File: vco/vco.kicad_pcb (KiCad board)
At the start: 2 copper layers, 59 parts, among them J1 Filtered Power, J13 Octave, J2 SQUARE OUT, J3 TRIANGLE OUT, J4 RAMP OUT, J5 1V/OCT, J6 CV, J7 SYNC, J8 PWM, J9 FM, U1 TL074, U2 TL072, U3 AS3340, U4 LM4040

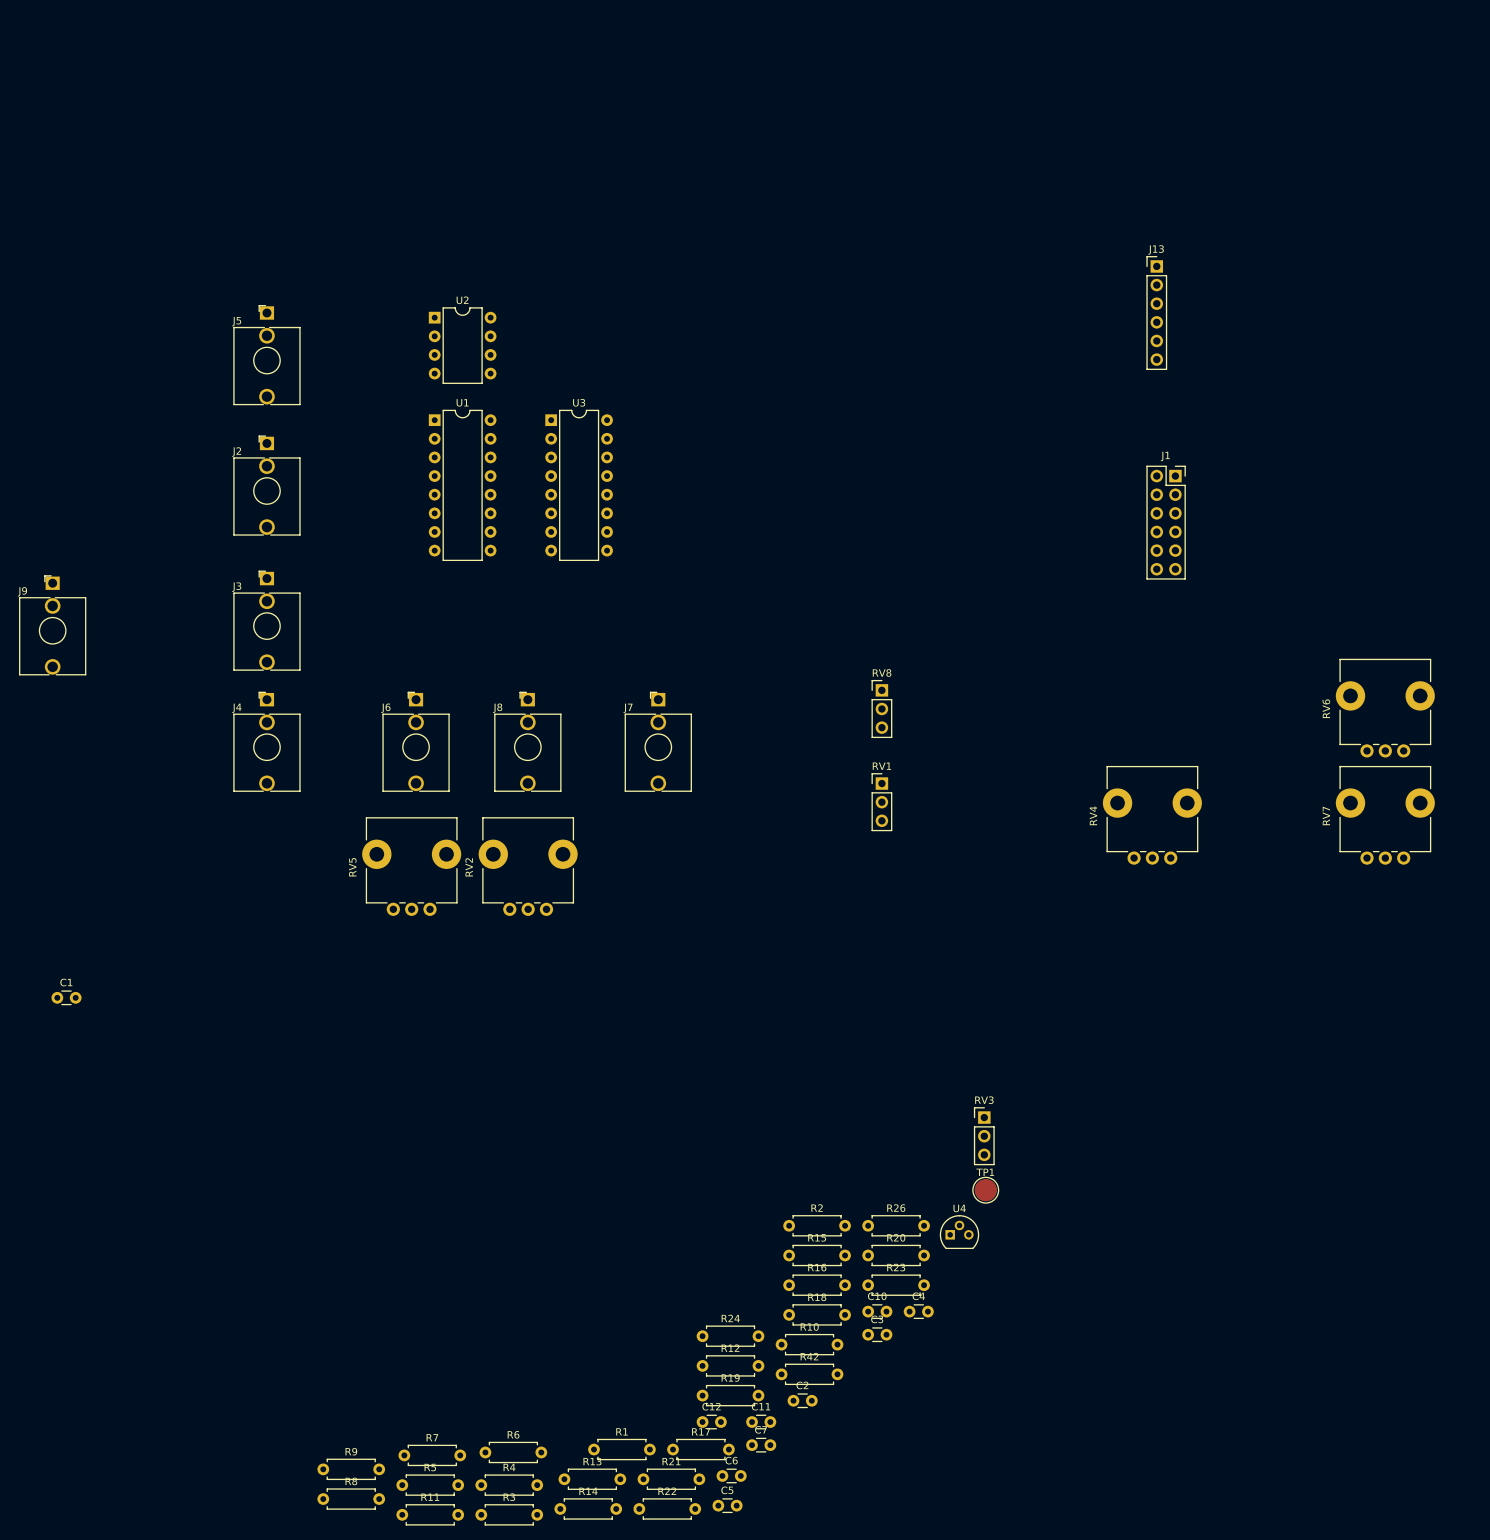
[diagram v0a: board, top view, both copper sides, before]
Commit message: Extra 7805 footprint, new standard, and some order to the VCO chaos
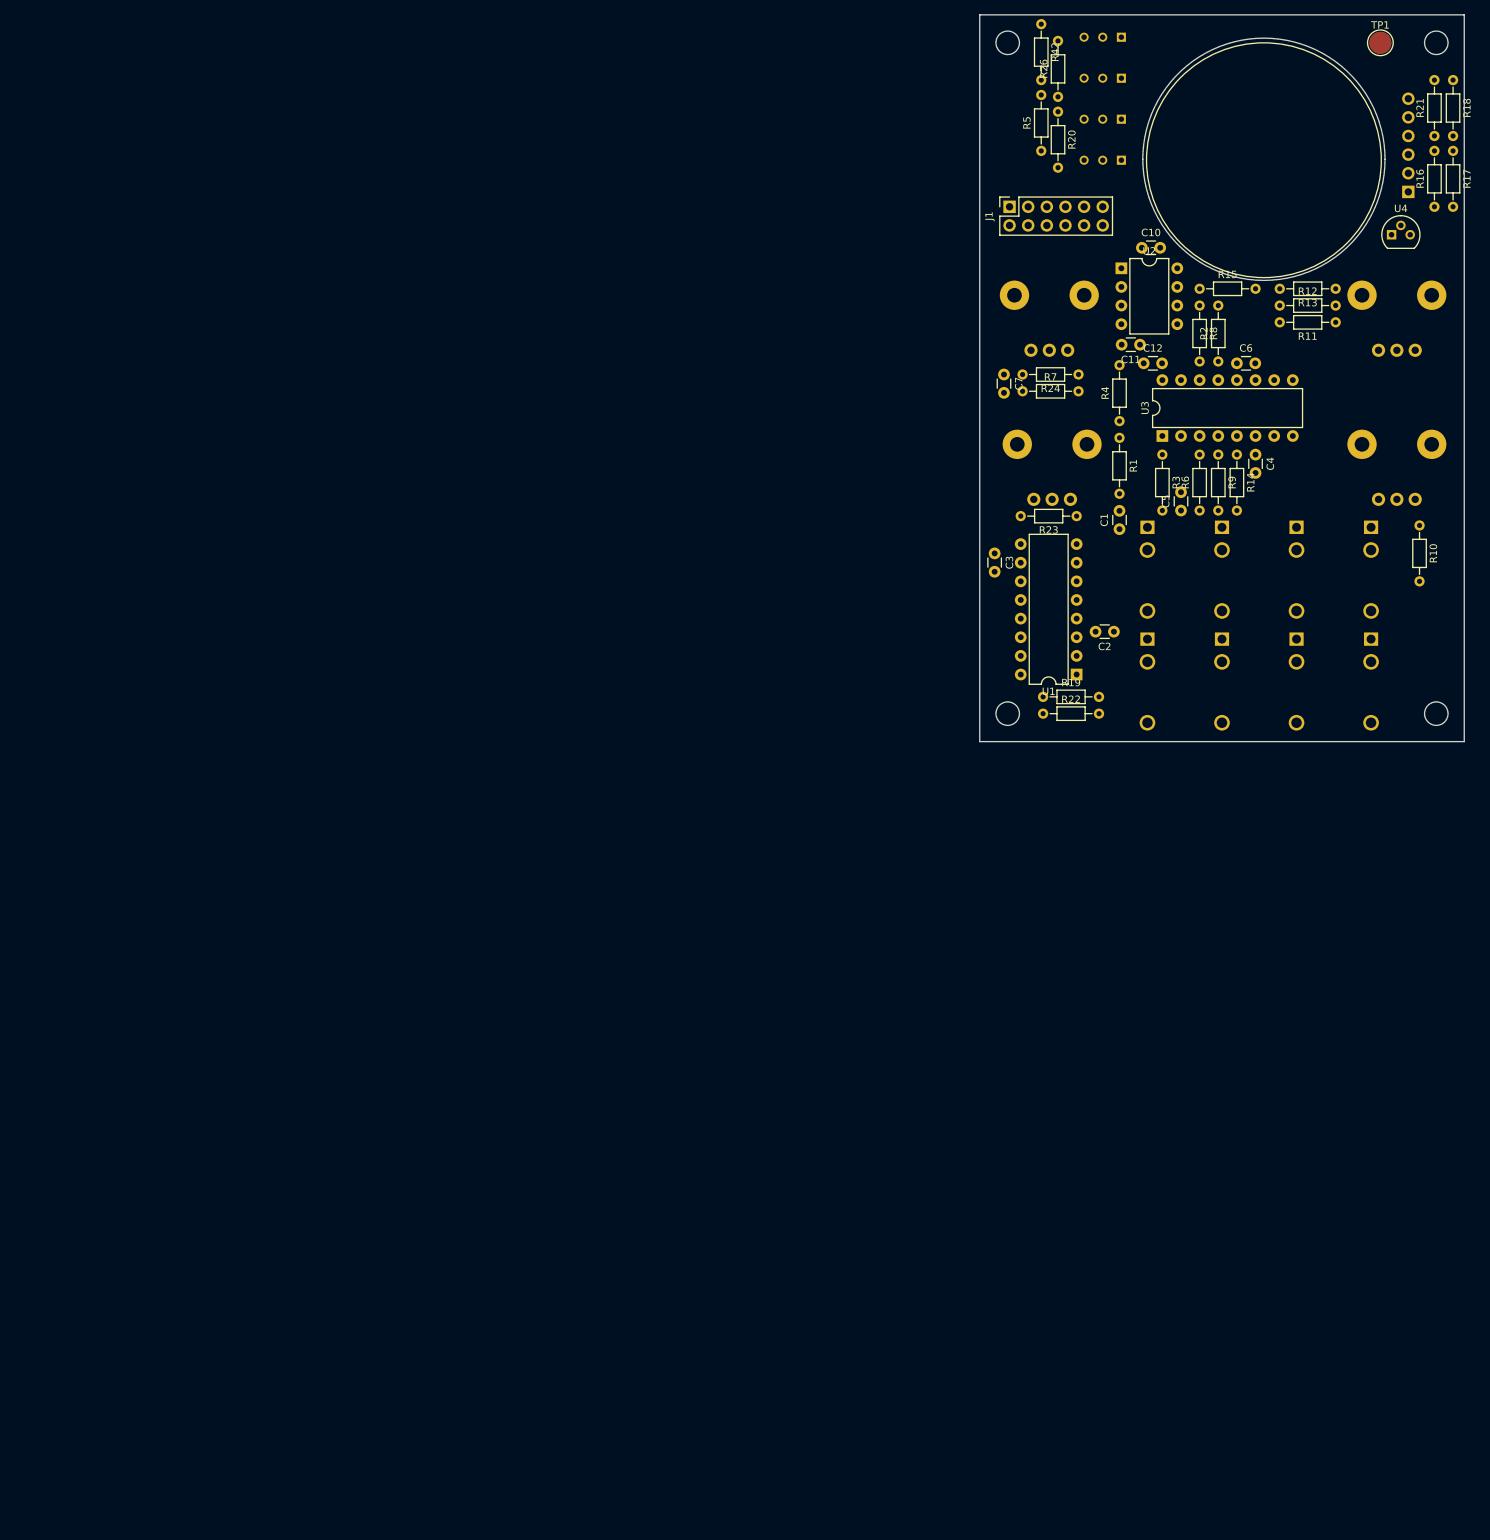
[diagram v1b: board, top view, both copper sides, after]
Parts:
- added H1: MountingHole, MountingHole:MountingHole_3.2mm_M3, F.Cu at (194.3, 31.8)
- added H2: MountingHole, MountingHole:MountingHole_3.2mm_M3, F.Cu at (194.3, 123.2)
- added H3: MountingHole, MountingHole:MountingHole_3.2mm_M3, F.Cu at (252.7, 31.8)
- added H4: MountingHole, MountingHole:MountingHole_3.2mm_M3, F.Cu at (252.7, 123.2)
- J13, J6, J8, J9, RV2, RV4, RV6, RV7: moved to B.Cu
- J2: value SQUARE OUT -> SQR; moved to B.Cu
- J3: value TRIANGLE OUT -> TRI; moved to B.Cu
- J4: value RAMP OUT -> RMP; moved to B.Cu
- J5: value 1V/OCT -> 1VO; moved to B.Cu
- J7: value SYNC -> SNC; moved to B.Cu
- R1, R10, R11, R12, R13, R14, R15, R16, R17, R18, R19, R2, R20, R21, R22, R23, R24, R26, R3, R4, R42, R5, R6, R7, R8, R9: footprint Resistor_THT:R_Axial_DIN0207_L6.3mm_D2.5mm_P7.62mm_Horizontal -> Resistor_THT:R_Axial_DIN0204_L3.6mm_D1.6mm_P7.62mm_Horizontal
- RV1, RV3, RV8: footprint Connector_PinHeader_2.54mm:PinHeader_1x03_P2.54mm_Vertical -> 3296W-1-250:TRIM_3296W-1-250; moved to B.Cu
- RV5: footprint Potentiometer_THT:Potentiometer_Alps_RK09L_Single_Vertical -> 3296W-1-250:TRIM_3296W-1-250; moved to B.Cu
- moved R21 212.5 mm to (252.5, 44.5), turned to 90 degrees
- moved R17 206.5 mm to (255.0, 46.5), turned to 270 degrees
- moved R11 206.4 mm to (239.0, 69.8), turned to 180 degrees
- moved R8 201.8 mm to (220.5, 67.6), turned to 270 degrees
- moved R5 201.6 mm to (198.9, 46.5), turned to 90 degrees
- moved R13 193.3 mm to (239.0, 65.3), turned to 180 degrees
- moved R18 191.1 mm to (255.0, 36.8), turned to 270 degrees
- moved R42 187.4 mm to (198.9, 29.2), turned to 270 degrees
- moved R9 184.4 mm to (223.0, 87.9), turned to 270 degrees
- moved R3 171.8 mm to (215.4, 87.9), turned to 270 degrees
- moved R16 171.3 mm to (252.5, 54.1), turned to 90 degrees
- moved R14 170.8 mm to (225.6, 87.9), turned to 270 degrees
- moved R4 169.1 mm to (209.6, 83.3), turned to 90 degrees
- moved R7 167.8 mm to (196.3, 79.2)
- moved C6 167.1 mm to (225.6, 75.4)
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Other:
- board outline added: 66 x 99.1 mm

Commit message: Settled at larger pcb, think its going to work with components placed like this
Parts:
- removed H2, H4: MountingHole, MountingHole:MountingHole_3.2mm_M3
- U1: footprint Package_DIP:DIP-16_W7.62mm -> Package_DIP:DIP-14_W7.62mm_Socket
- U2: footprint Package_DIP:DIP-8_W7.62mm -> Package_DIP:DIP-8_W7.62mm_Socket
- U3: footprint Package_DIP:DIP-16_W7.62mm -> Package_DIP:DIP-16_W7.62mm_Socket
- moved J6 164.3 mm to (83.3, 147.8), turned to 270 degrees
- moved RV5 149.1 mm to (89.2, 138.7), turned to 0 degrees
- moved R20 143.0 mm to (92.7, 134.4), turned to 180 degrees
- moved RV1 140.3 mm to (89.2, 117.9), turned to 0 degrees
- moved C12 127.3 mm to (86.4, 90.2), turned to 90 degrees
- moved C4 127.1 mm to (101.9, 102.6)
- moved R6 127.1 mm to (94.2, 110.2)
- moved R14 127.1 mm to (99.3, 102.6)
- moved R3 127.1 mm to (89.2, 102.6)
- moved R9 127.1 mm to (96.8, 102.6)
- moved U3 127.1 mm to (89.2, 100.1)
- moved R8 127.1 mm to (94.2, 82.0)
- moved R2 127.1 mm to (96.8, 89.7)
- moved C6 127.0 mm to (99.3, 89.7)
- moved R15 125.9 mm to (101.9, 107.4), turned to 270 degrees
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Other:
- board size 66 x 99.1 mm -> 99.1 x 99.1 mm

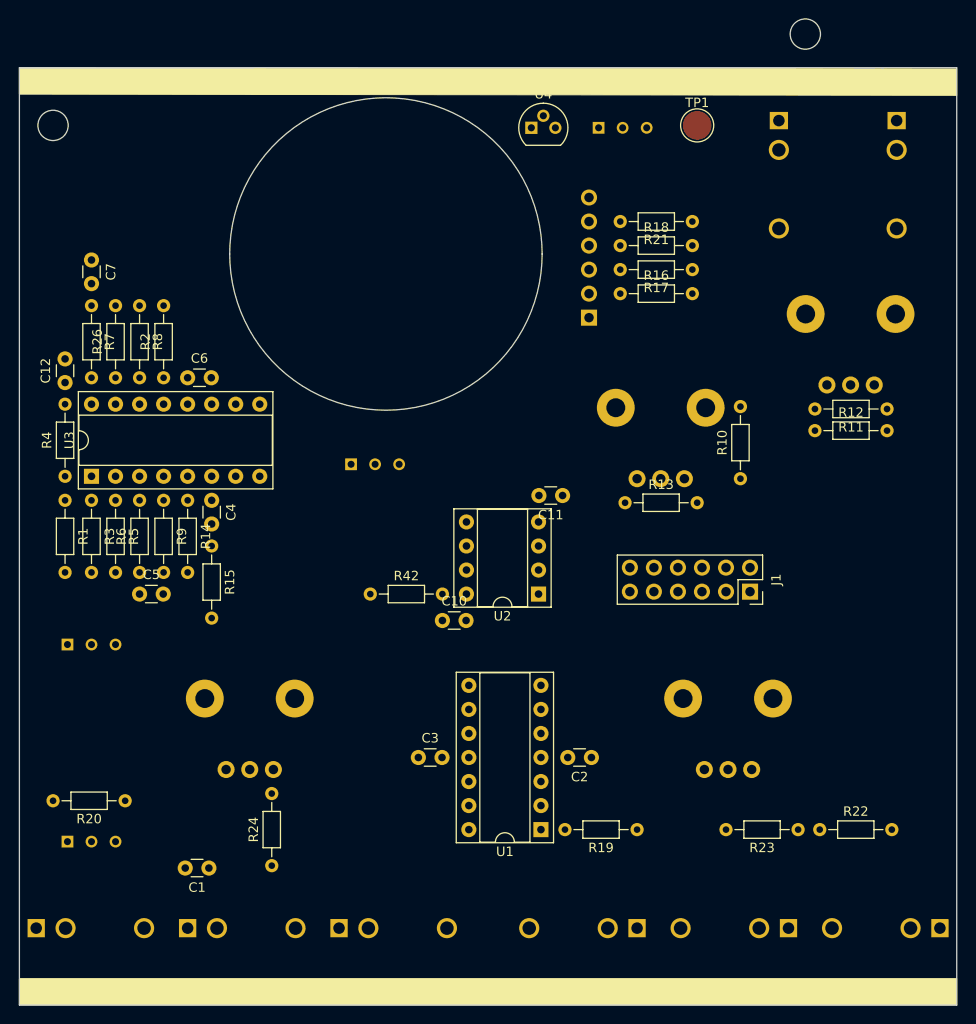
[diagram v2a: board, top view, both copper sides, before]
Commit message: All wired up, slightly different layout
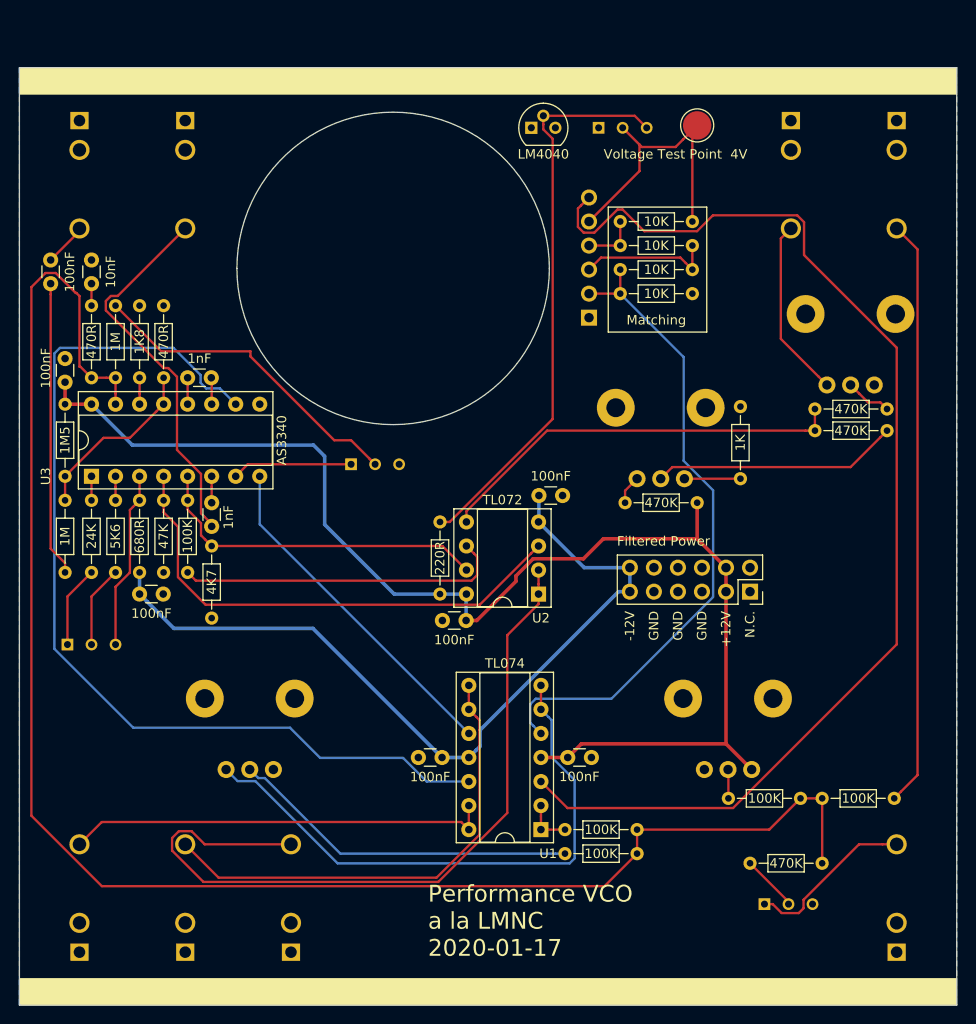
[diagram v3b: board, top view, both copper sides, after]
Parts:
- removed H1, H3: MountingHole, MountingHole:MountingHole_3.2mm_M3
- RV1: value 10K -> 10K Track
- RV5: value 10OK -> 10OK CVLVL
- RV8: value 20K -> 20K HFTRACK
- moved J6 91.0 mm to (174.2, 150.4), turned to 0 degrees
- moved J7 86.9 mm to (99.1, 62.5), turned to 180 degrees
- moved J9 86.1 mm to (87.9, 62.5), turned to 180 degrees
- moved R20 74.0 mm to (166.4, 141.0)
- moved RV5 74.0 mm to (162.8, 145.3)
- moved J2 68.6 mm to (110.2, 150.4), turned to 0 degrees
- moved C1 66.4 mm to (84.8, 77.2), turned to 270 degrees
- moved J4 63.8 mm to (99.1, 150.4), turned to 0 degrees
- moved J3 59.0 mm to (87.9, 150.4), turned to 0 degrees
- moved R24 38.6 mm to (146.8, 140.0), turned to 180 degrees
- moved R42 10.6 mm to (126.0, 104.9), turned to 270 degrees
- moved R22 3.31 mm to (166.4, 134.1)
- moved R23 3.31 mm to (164.1, 134.1)
- moved C12 2.54 mm to (86.4, 87.6), turned to 270 degrees
- moved J8 1.27 mm to (163.1, 62.5)
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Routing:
- net CVINPUTS: track 0.00 -> 176.0 mm
- net +12V: track 0.00 -> 139.2 mm
- net Net-(J13-Pad6): track 0.00 -> 125.3 mm
- net VTO: track 0.00 -> 103.2 mm
- net -12V: track 0.00 -> 86.5 mm
- net SQUAREOUT: track 0.00 -> 81.6 mm
- net 1V: track 0.00 -> 69.5 mm
- net 1VOCTIN: track 0.00 -> 62.2 mm
- net Net-(RV7-Pad1): track 0.00 -> 60.9 mm
- net Net-(R42-Pad1): track 0.00 -> 60.3 mm
- net VP: track 0.00 -> 53.2 mm
- net RAMPOUT: track 0.00 -> 50.7 mm
- net TRIANGLEOUT: track 0.00 -> 45.0 mm
- net Net-(R11-Pad2): track 0.00 -> 43.8 mm
- net SYNCIN1: track 0.00 -> 40.1 mm
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- added copper zone on B.Cu, net GND
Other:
- outline, holes or cut-outs redrawn
- board text added: "+12V"
- board text added: "-12V"
- board text added: "0V"
- board text added: "1V"
- board text added: "2V"
- board text added: "3V"
- board text added: "4V"
- board text added: "C"
- board text added: "GND"
- board text added: "Matching"
- board text added: "N.C."
- board text added: "OSC OUTPUTS"
- board text added: "Performance VCO a la LMNC 2020-01-17"

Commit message: Started with the panel
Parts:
- added C8: 10uF, Capacitor_THT:CP_Radial_D5.0mm_P2.50mm, F.Cu at (166.6, 106.9)
- added C9: 10uF, Capacitor_THT:CP_Radial_D5.0mm_P2.50mm, F.Cu at (141.7, 120.1)
- J1: value Filtered Power -> Power; footprint Connector_PinSocket_2.54mm:PinSocket_2x06_P2.54mm_Vertical -> Connector_PinHeader_2.54mm:PinHeader_2x05_P2.54mm_Vertical
- moved J1 3.59 mm to (156.2, 109.7)
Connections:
- J1 pad 1: Net-(J1-Pad1) -> +12V
- J1 pad 10: GND -> -12V
- J1 pad 2: Net-(J1-Pad2) -> +12V
- J1 pad 3: +12V -> GND
- J1 pad 4: +12V -> GND
- J1 pad 9: GND -> -12V
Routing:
- net +12V: track 139.2 -> 151.4 mm
- net -12V: track 86.5 -> 95.1 mm
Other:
- board text removed: "N.C."
